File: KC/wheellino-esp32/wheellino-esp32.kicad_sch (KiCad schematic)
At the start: 29 parts, among them J1 SR04, J2 Servo, J3 Motor Drivers, J4 Motor Sensors, J5 Contact Sensors, J6 12V, J7 5V, J8 GY521, J9 LCD, U1 3V3, U2 ESP32-DevKitC

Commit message: Esp32 board
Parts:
- removed C6: 1n, Capacitor_THT:C_Rect_L7.0mm_W2.0mm_P5.00mm, symbol Device:C
- added C6: 22uF, Capacitor_THT:CP_Radial_D5.0mm_P2.50mm, symbol Device:C_Polarized
- added C7, C8: 1n, Capacitor_THT:C_Rect_L7.0mm_W2.0mm_P5.00mm, symbol Device:C
- added R8, R9: 10K, Resistor_THT:R_Axial_DIN0207_L6.3mm_D2.5mm_P10.16mm_Horizontal, symbol Device:R
- R1, R2, R3, R4, R7: value 1K -> 220
- R5: value 10K -> 100K
- R6: value 2K -> 22K
- U2: footprint Espressif:ESP32-DevKitC -> Whellino:ESP32
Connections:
- net +3V3: now also J4.1 (Pin_1), J4.2 (Pin_2), R8.1, R9.1
- net +5VD: now also J1.1 (Pin_1), J2.2 (Pin_2), J3.2 (Pin_2), J3.8 (Pin_8), J9.3 (Pin_3)
- net GND: now also J1.4 (Pin_4), J2.1 (Pin_1), J3.4 (Pin_4), J3.6 (Pin_6), J4.3 (Pin_3), J4.4 (Pin_4), J5.2 (Pin_2), J5.4 (Pin_4), J9.4 (Pin_4), C6.2, C7.2, C8.2
- net at R1.1: now also J3.3 (Pin_3), U2.28 (GPIO17)
- net at U2.15 (MTCK/GPIO13/ADC2_CH4): now also J2.3 (Pin_3)
- net at U2.2 (CHIP_PU): now also C6.1
- net at U2.27 (GPIO16): now also J3.1 (Pin_1), R2.1
- net at U2.3 (SENSOR_VP/GPIO36/ADC1_CH0): now also J5.1 (Pin_1), C8.1, R9.2
- net at U2.30 (GPIO18): now also J3.7 (Pin_7), R4.1
- net at U2.31 (GPIO19): now also J3.5 (Pin_5), R3.1
- net at U2.33 (GPIO21): now also J8.4 (Pin_4), J9.2 (Pin_2)
- net at U2.36 (GPIO22): now also J8.3 (Pin_3), J9.1 (Pin_1)
- net at U2.37 (GPIO23): now also J1.2 (Pin_2)
- net at U2.4 (SENSOR_VN/GPIO39/ADC1_CH3): now also C5.1, R5.2, R6.1
- net at U2.5 (VDET_1/GPIO34/ADC1_CH6): now also J1.3 (Pin_3)
- net at U2.6 (VDET_2/GPIO35/ADC1_CH7): now also J5.3 (Pin_3), C7.1, R8.2
- net at U2.7 (32K_XP/GPIO32/ADC1_CH4): now also J4.5 (Pin_5)
- net at U2.8 (32K_XN/GPIO33/ADC1_CH5): now also J4.6 (Pin_6)
- net at U2.9 (DAC_1/ADC2_CH8/GPIO25): now also R7.1
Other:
- title: (none) -> Whellino ESP32
- moved on the sheet: C5, D1, D2, D3, D4, D5, J1, J2, J3, J4, J5, J6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

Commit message: reordered
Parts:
- removed C7, C8: 1n, Capacitor_THT:C_Rect_L7.0mm_W2.0mm_P5.00mm, symbol Device:C
- added C1, C2: 1uF, Capacitor_THT:CP_Radial_D5.0mm_P2.50mm, symbol Device:C_Polarized
- renumbered C5 to C3, C6 to C4, C1 to C5, C2 to C6, C3 to C7, C4 to C8, J4 to J1, J5 to J2, J1 to J3, J2 to J4, J8 to J5, J3 to J6, J9 to J7, J6 to J8, J7 to J9, R8 to R1, R9 to R2, R5 to R3, R6 to R4, R1 to R5, R2 to R6, R3 to R7, R4 to R8, R7 to R9, U2 to U1, U1 to U2
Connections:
- net +3V3: now also U2.2 (VOUT); no longer U2.3 (VOUT)
- net GND: now also U2.3 (GND), C1.2, C2.2; no longer U2.2 (GND)
- net at J2.1 (Pin_1), R2.2, U1.3 (SENSOR_VP/GPIO36/ADC1_CH0): now also C2.1
- net at J2.3 (Pin_3), R1.2, U1.6 (VDET_2/GPIO35/ADC1_CH7): now also C1.1

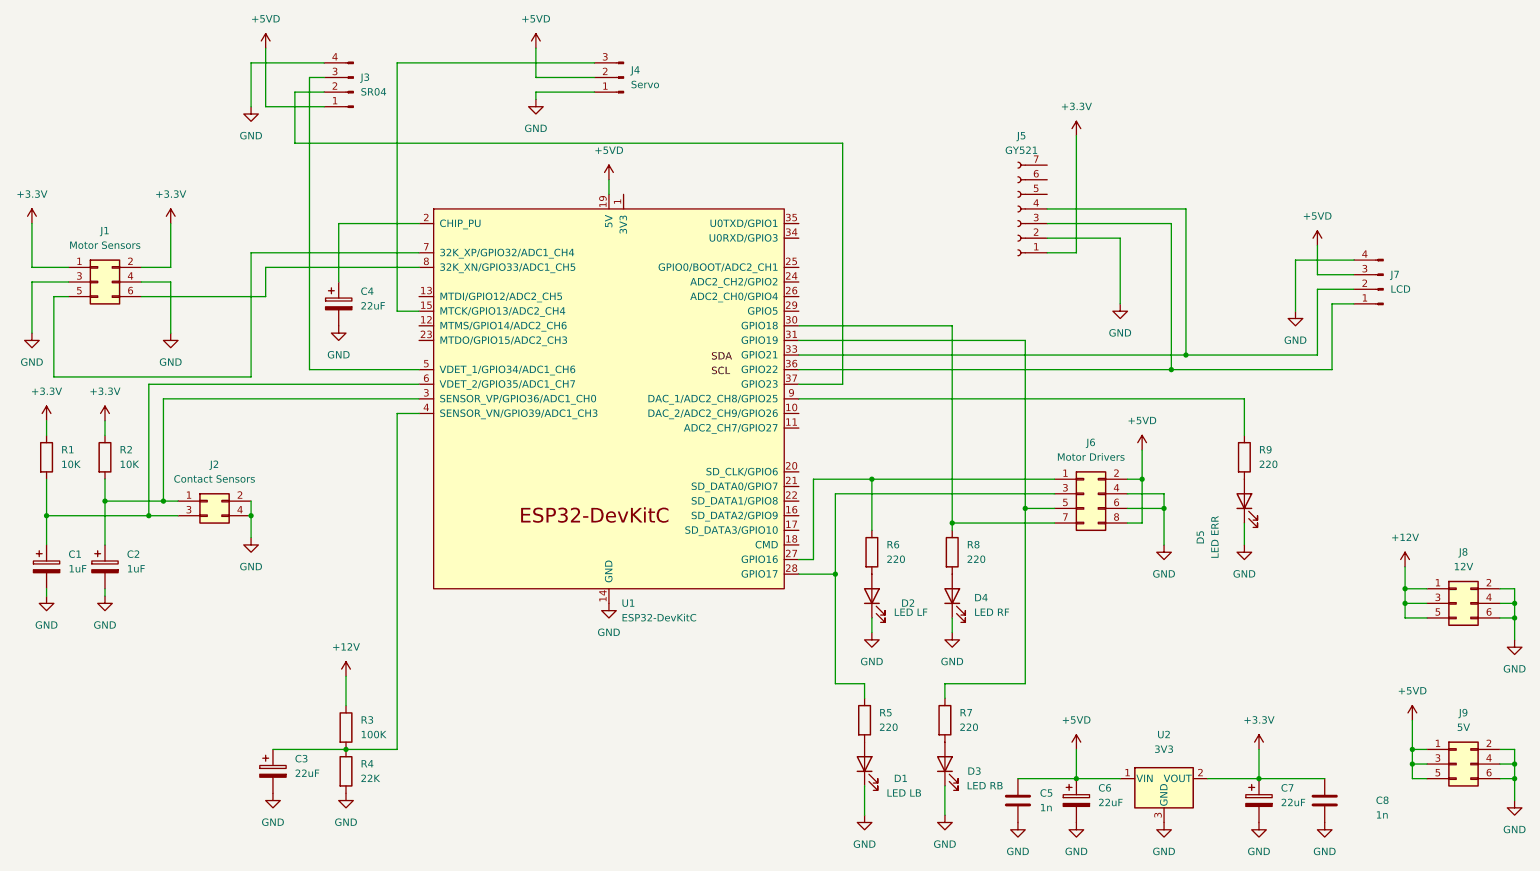
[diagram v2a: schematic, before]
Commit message: flip camera image Lidar signals LidarServo head cad projects Add lidar
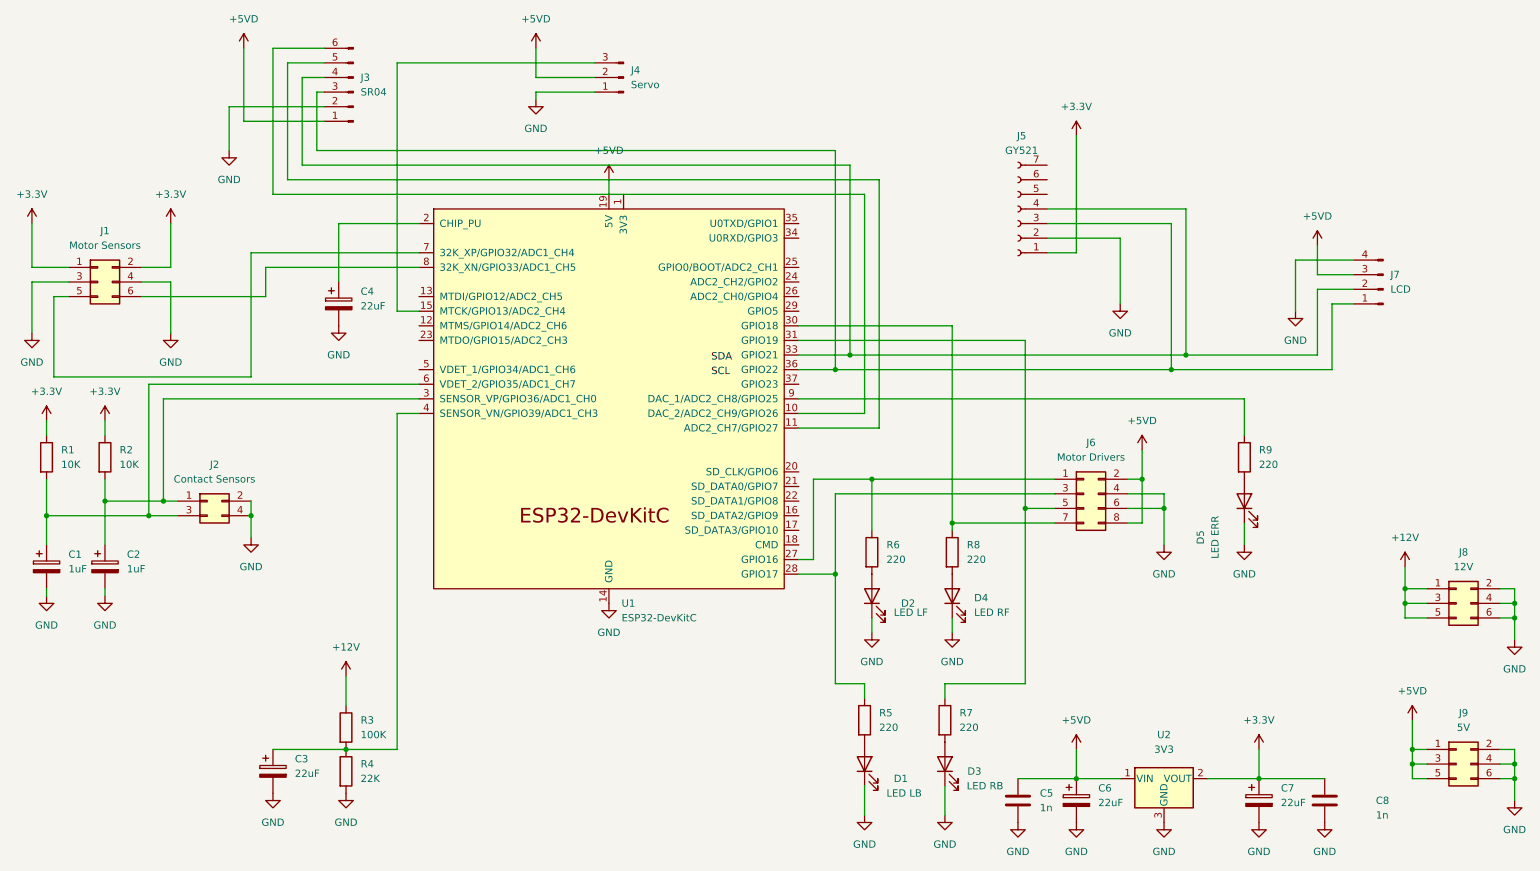
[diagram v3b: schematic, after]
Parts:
- J3: footprint Connector_PinHeader_2.54mm:PinHeader_1x04_P2.54mm_Vertical -> Connector_PinHeader_2.54mm:PinHeader_1x06_P2.54mm_Vertical; symbol Connector:Conn_01x04_Pin -> Connector:Conn_01x06_Pin
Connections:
- net GND: now also J3.2 (Pin_2); no longer J3.4 (Pin_4)
- net at U1.10 (DAC_2/ADC2_CH9/GPIO26): now also J3.6 (Pin_6)
- net at U1.11 (ADC2_CH7/GPIO27): now also J3.5 (Pin_5)
- net at J5.4 (Pin_4), J7.2 (Pin_2), U1.33 (GPIO21): now also J3.4 (Pin_4)
- net at J5.3 (Pin_3), J7.1 (Pin_1), U1.36 (GPIO22): now also J3.3 (Pin_3)
- net at U1.37 (GPIO23): no longer J3.2 (Pin_2)
- net at U1.5 (VDET_1/GPIO34/ADC1_CH6): no longer J3.3 (Pin_3)
